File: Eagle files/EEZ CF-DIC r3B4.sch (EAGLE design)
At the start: 240 parts, among them IC1 MC79L05, IC2 LP2951, IC3 VIPer35L, IC4 SI8233BB-D-IS1, IC5 LM5041B, IC6 IR11688STRPBF, IC7 TL072, IC8 TL103W, IC9 TL431, P1 T910W-50K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

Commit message: Optional temperature alarm
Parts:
- added C75: 100n, rcl:C-EUC0603
- added IC10: LM211PWR, EEZ_Lib1:LM211
- added NTC1: 10K, EEZ_Lib1:NTCR_0805
- added R81: 100K, rcl:R-EU_R0805
- added R82, R84: 10K, rcl:R-EU_R0805
- added R83: N.C., rcl:R-EU_R0805
- R15: value N.C. -> 10K
- R16: value 10K -> N.C.
- R80: value N.C. -> 1K
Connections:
- new net +2.5VREF: C72.1, IC8-1.+IN1, NTC1.P$1, P1.E, R66.2, R72.1, R80.2
- new net N$34: IC10A.-IN, NTC1.P$2, R84.2
- net AUX: now also R16.2; no longer R15.2
- net FB: now also R83.2; no longer R80.2
- net GND: now also C75.2, IC10A.E, IC10P.V-, R82.2, R83.1, R84.1; no longer R80.1
- net N$141: now also R16.1; no longer R15.1
- net N$7: now also IC10A.+IN, R80.1, R81.2, R82.1; no longer C72.1, IC8-1.+IN1, P1.E, R66.2, R72.1
- net PWRGOOD: now also IC10A.C, R15.2, R81.1; no longer R16.2
- net V+: now also C75.1, IC10P.V+, R15.1; no longer R16.1
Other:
- note added: "+5 Vdc 5"
- note added: "+5 Vdc 7"
- note added: "-9 Vdc 8"
- note added: "AC line 2"
- note added: "AC neutral 3"
- note added: "Bias+ 3"
- note added: "Bias- 2"
- note added: "Earth (PE) 1"
- note added: "GND 2"
- note added: "GND 6"
- note added: "PWRGOOD 4"
- note added: "R65+R71"
- note added: "R76"
- note added: "Temperature alarm (optional)"
- note added: "U_MON 1"
- note added: "Vout+ 1"
- note added: "X2 3-pin input connector"
- note added: "X3 8-pin output connector"
- note added: "X4 2-pin output connector"
- note removed: "R64+R70"
- note removed: "R75"
- moved on the sheet: C52, C53, C54, C55, C56, C57, C58, C59, C60, C61, C62, C63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

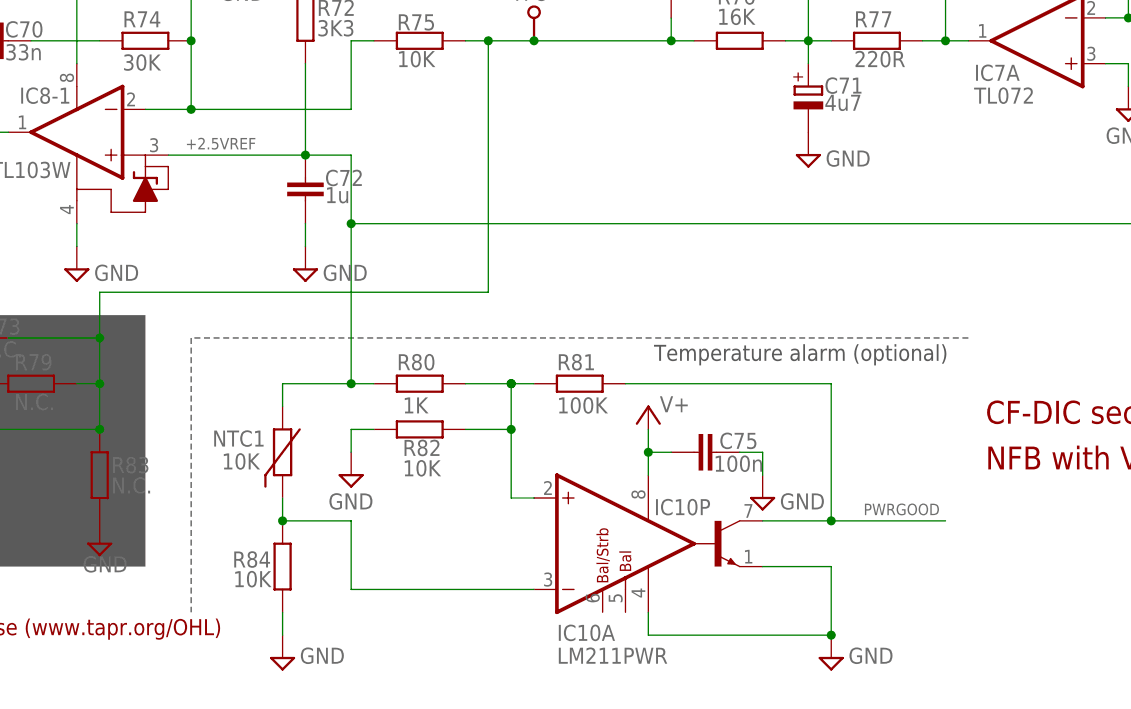
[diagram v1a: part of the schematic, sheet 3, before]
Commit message: New values for temp. comparator
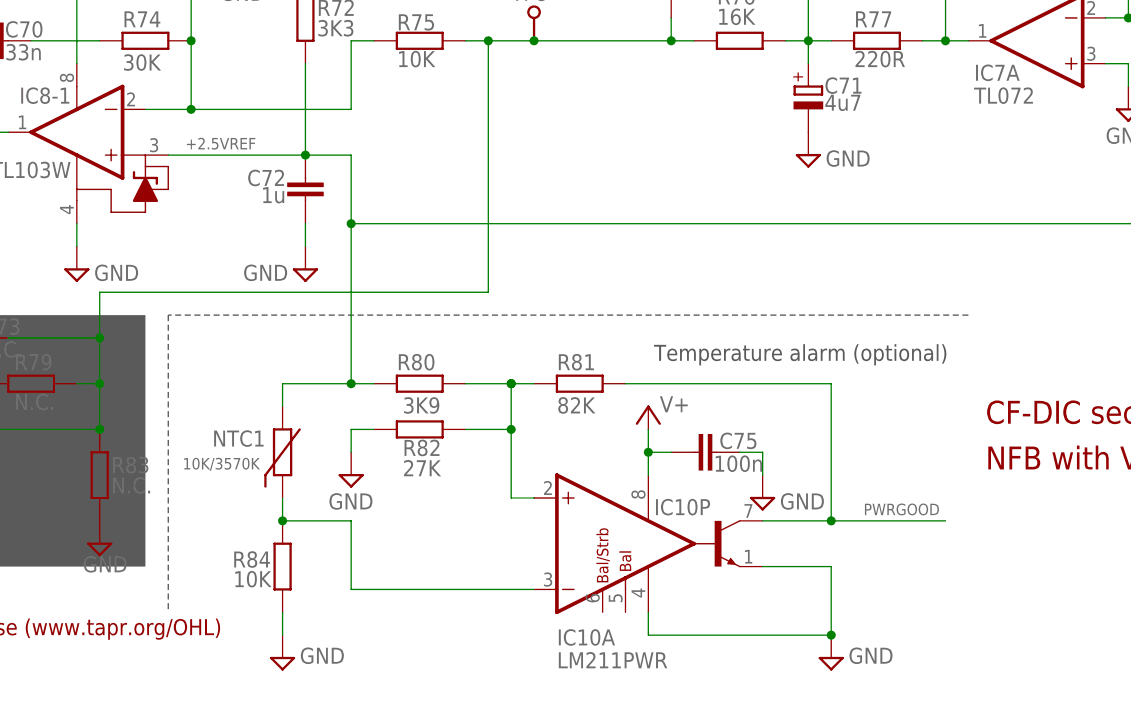
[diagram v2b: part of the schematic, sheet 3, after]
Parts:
- NTC1: value 10K -> 10K/3570K
- R80: value 1K -> 3K9
- R81: value 100K -> 82K
- R82: value 10K -> 27K
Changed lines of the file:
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@@
 <part name="P+2" library="supply2" deviceset="V+" device=""/>
 <part name="IC10" library="EEZ_Lib1" deviceset="LM211" device="" value="LM211PWR"/>
-<part name="NTC1" library="EEZ_Lib1" deviceset="NTC" device="R_0805" value="10K"/>
+<part name="NTC1" library="EEZ_Lib1" deviceset="NTC" device="R_0805" value="10K/3570K"/>
 <part name="R84" library="rcl" deviceset="R-EU_" device="R0805" value="10K"/>
 <part name="SUPPLY25" library="supply2" deviceset="GND" device=""/>
 <part name="SUPPLY26" library="supply2" deviceset="GND" device=""/>
-<part name="R80" library="rcl" deviceset="R-EU_" device="R0805" value="1K"/>
-<part name="R81" library="rcl" deviceset="R-EU_" device="R0805" value="100K"/>
-<part name="R82" library="rcl" deviceset="R-EU_" device="R0805" value="10K"/>
+<part name="R80" library="rcl" deviceset="R-EU_" device="R0805" value="3K9"/>
+<part name="R81" library="rcl" deviceset="R-EU_" device="R0805" value="82K"/>
+<part name="R82" library="rcl" deviceset="R-EU_" device="R0805" value="27K"/>
 <part name="SUPPLY21" library="supply2" deviceset="GND" device=""/>
 </parts>
@@
 <text x="224.155" y="172.085" size="1.778" layer="101">X4 2-pin output connector</text>
 <wire x1="223.52" y1="134.62" x2="226.06" y2="134.62" width="0.1524" layer="97" style="shortdash"/>
-<wire x1="162.56" y1="40.64" x2="76.2" y2="40.64" width="0.1524" layer="97" style="shortdash"/>
+<wire x1="162.56" y1="43.18" x2="73.66" y2="43.18" width="0.1524" layer="97" style="shortdash"/>
 <text x="127.635" y="38.1" size="1.778" layer="97">Temperature alarm (optional)</text>
-<wire x1="76.2" y1="40.64" x2="76.2" y2="10.16" width="0.1524" layer="97" style="shortdash"/>
+<wire x1="73.66" y1="43.18" x2="73.66" y2="10.16" width="0.1524" layer="97" style="shortdash"/>
 </plain>
 <instances>
@@
 </instance>
 <instance part="C72" gate="G$1" x="88.9" y="58.42" smashed="yes">
-<attribute name="NAME" x="91.059" y="57.531" size="1.778" layer="95"/>
-<attribute name="VALUE" x="91.059" y="55.626" size="1.778" layer="96"/>
+<attribute name="NAME" x="86.741" y="57.531" size="1.778" layer="95" rot="MR0"/>
+<attribute name="VALUE" x="86.741" y="55.626" size="1.778" layer="96" rot="MR0"/>
 </instance>
 <instance part="SUPPLY5" gate="GND" x="88.9" y="48.26" smashed="yes">
-<attribute name="VALUE" x="90.805" y="46.99" size="1.778" layer="96"/>
+<attribute name="VALUE" x="86.995" y="46.99" size="1.778" layer="96" rot="MR0"/>
 </instance>
 <instance part="R74" gate="G$1" x="71.12" y="73.66" smashed="yes" rot="R180">
@@
 </instance>
 <instance part="IC10" gate="A" x="124.46" y="17.78" smashed="yes">
-<attribute name="NAME" x="116.84" y="6.985" size="1.778" layer="95"/>
-<attribute name="VALUE" x="116.84" y="4.445" size="1.778" layer="96"/>
+<attribute name="NAME" x="116.84" y="8.255" size="1.778" layer="95" rot="MR180"/>
+<attribute name="VALUE" x="116.84" y="5.715" size="1.778" layer="96" rot="MR180"/>
 </instance>
 <instance part="NTC1" gate="G$1" x="86.36" y="27.94" smashed="yes">
 <attribute name="NAME" x="84.455" y="28.575" size="1.778" layer="95" rot="MR0"/>
-<attribute name="VALUE" x="83.82" y="26.035" size="1.778" layer="96" rot="MR0"/>
+<attribute name="VALUE" x="83.82" y="26.035" size="1.27" layer="96" rot="MR0"/>
 </instance>
 <instance part="R84" gate="G$1" x="86.36" y="15.24" smashed="yes" rot="MR90">
